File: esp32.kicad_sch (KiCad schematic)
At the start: 15 parts, among them J2 Conn_01x05_Pin, Q3 MMBT3904, Q4 MMBT3904, U14 S32K324NHT1MPBST, Y1 ECS-2520MV-xxx-xx

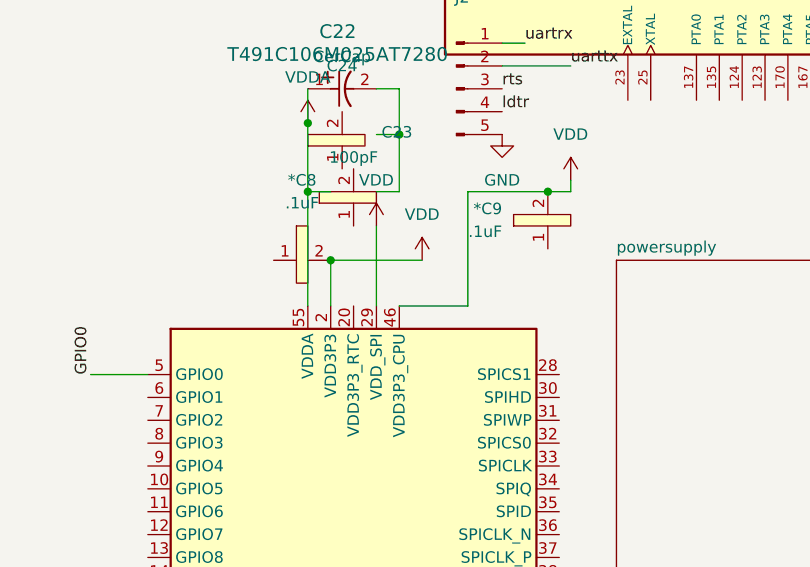
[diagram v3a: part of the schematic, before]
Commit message: loaded the power symbol library back in
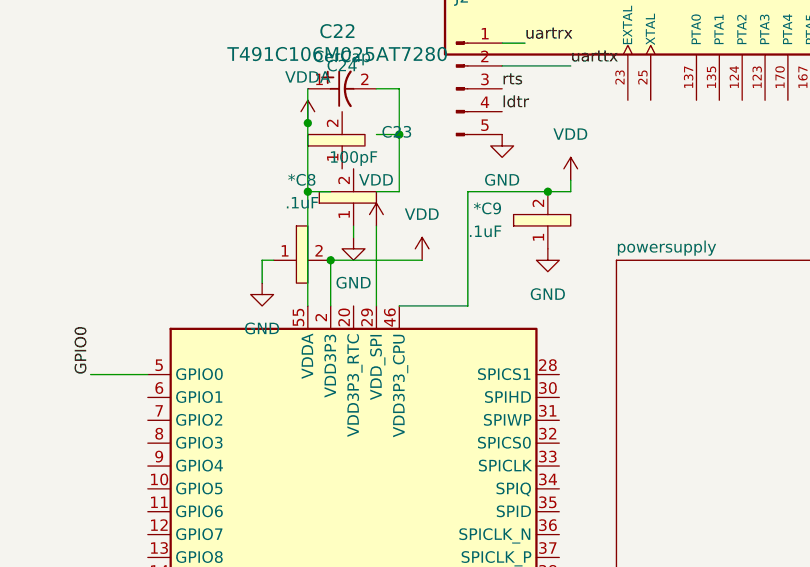
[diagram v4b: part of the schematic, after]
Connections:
- net GND: now also *C8.1, *C9.1, C23.1
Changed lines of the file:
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@@
+	(wire
+		(pts
+			(xy 128.27 73.66) (xy 129.54 73.66)
+		)
+		(stroke
+			(width 0)
+			(type default)
+		)
+	)
 	(wire
 		(pts
@@
 	(wire
 		(pts
+			(xy 138.43 71.12) (xy 138.43 69.85)
+		)
+		(stroke
+			(width 0)
+			(type default)
+		)
+	)
+	(wire
+		(pts
 			(xy 104.14 147.32) (xy 115.57 147.32)
 		)
@@
 		(pts
 			(xy 115.57 138.43) (xy 110.49 138.43)
+		)
+		(stroke
+			(width 0)
+			(type default)
+		)
+	)
+	(wire
+		(pts
+			(xy 128.27 76.2) (xy 128.27 73.66)
 		)
 		(stroke
@@
 	)
 	(symbol
+		(lib_id "powerSYMB:GND")
+		(at 160.02 72.39 0)
+		(unit 1)
+		(exclude_from_sim no)
+		(in_bom yes)
+		(on_board yes)
+		(dnp no)
+		(fields_autoplaced yes)
+		(property "Reference" "#PWR60"
+			(at 160.02 78.74 0)
+			(effects
+				(font
+					(size 1.27 1.27)
+				)
+				(hide yes)
+			)
+		)
+		(property "Value" "GND"
+			(at 160.02 77.47 0)
+			(effects
+				(font
+					(size 1.27 1.27)
+				)
+			)
+		)
+		(property "Footprint" ""
+			(at 160.02 72.39 0)
+			(effects
+				(font
+					(size 1.27 1.27)
+				)
+				(hide yes)
+			)
+		)
+		(property "Datasheet" ""
+			(at 160.02 72.39 0)
+			(effects
+				(font
+					(size 1.27 1.27)
+				)
+				(hide yes)
+			)
+		)
+		(property "Description" "Power symbol creates a global label with name \"GND\" , ground"
+			(at 160.02 72.39 0)
+			(effects
+				(font
+					(size 1.27 1.27)
+				)
+				(hide yes)
+			)
+		)
+		(pin "1"
+		)
+		(instances
+			(project ""
+				(path "/c4754426-a41b-4341-9d09-2e389619f3d6"
+					(reference "#PWR60")
+					(unit 1)
+				)
+			)
+		)
+	)
+	(symbol
 		(lib_id "esp32lib:myEsp32")
 		(at 135.89 101.6 0)
@@
 	)
 	(symbol
+		(lib_id "powerSYMB:GND")
+		(at 128.27 76.2 0)
+		(unit 1)
+		(exclude_from_sim no)
+		(in_bom yes)
+		(on_board yes)
+		(dnp no)
+		(fields_autoplaced yes)
+		(property "Reference" "#PWR61"
+			(at 128.27 82.55 0)
+			(effects
+				(font
+					(size 1.27 1.27)
+				)
+				(hide yes)
+			)
+		)
+		(property "Value" "GND"
+			(at 128.27 81.28 0)
+			(effects
+				(font
+					(size 1.27 1.27)
+				)
+			)
+		)
+		(property "Footprint" ""
+			(at 128.27 76.2 0)
+			(effects
+				(font
+					(size 1.27 1.27)
+				)
+				(hide yes)
+			)
+		)
+		(property "Datasheet" ""
+			(at 128.27 76.2 0)
+			(effects
+				(font
+					(size 1.27 1.27)
+				)
+				(hide yes)
+			)
+		)
+		(property "Description" "Power symbol creates a global label with name \"GND\" , ground"
+			(at 128.27 76.2 0)
+			(effects
+				(font
+					(size 1.27 1.27)
+				)
+				(hide yes)
+			)
+		)
+		(pin "1"
+		)
+		(instances
+			(project ""
+				(path "/c4754426-a41b-4341-9d09-2e389619f3d6"
+					(reference "#PWR61")
+					(unit 1)
+				)
+			)
+		)
+	)
+	(symbol
 		(lib_id "Oscillator:ECS-2520MV-xxx-xx")
 		(at 80.01 132.08 0)
@@
 					(unit 1)
 				)
+			)
+		)
+	)
+	(symbol
+		(lib_id "powerSYMB:GND")
+		(at 138.43 71.12 0)
+		(unit 1)
+		(exclude_from_sim no)
+		(in_bom yes)
+		(on_board yes)
+		(dnp no)
+		(fields_autoplaced yes)
+		(property "Reference" "#PWR89"
+			(at 138.43 77.47 0)
+			(effects
+				(font
+					(size 1.27 1.27)
+				)
+				(hide yes)
+			)
+		)
+		(property "Value" "GND"
+			(at 138.43 76.2 0)
+			(effects
+				(font
+					(size 1.27 1.27)
+				)
+			)
+		)
+		(property "Footprint" ""
+			(at 138.43 71.12 0)
+			(effects
+				(font
+					(size 1.27 1.27)
+				)
+				(hide yes)
+			)
+		)
+		(property "Datasheet" ""
+			(at 138.43 71.12 0)
+			(effects
+				(font
+					(size 1.27 1.27)
+				)
+				(hide yes)
+			)
+		)
+		(property "Description" "Power symbol creates a global label with name \"GND\" , ground"
+			(at 138.43 71.12 0)
+			(effects
+				(font
+					(size 1.27 1.27)
+				)
+				(hide yes)
+			)
+		)
+		(pin "1"
+		)
+		(instances
+			(project ""
+				(path "/c4754426-a41b-4341-9d09-2e389619f3d6"
+					(reference "#PWR89")
+					(unit 1)
+				)
